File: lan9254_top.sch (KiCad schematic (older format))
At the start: 2 parts

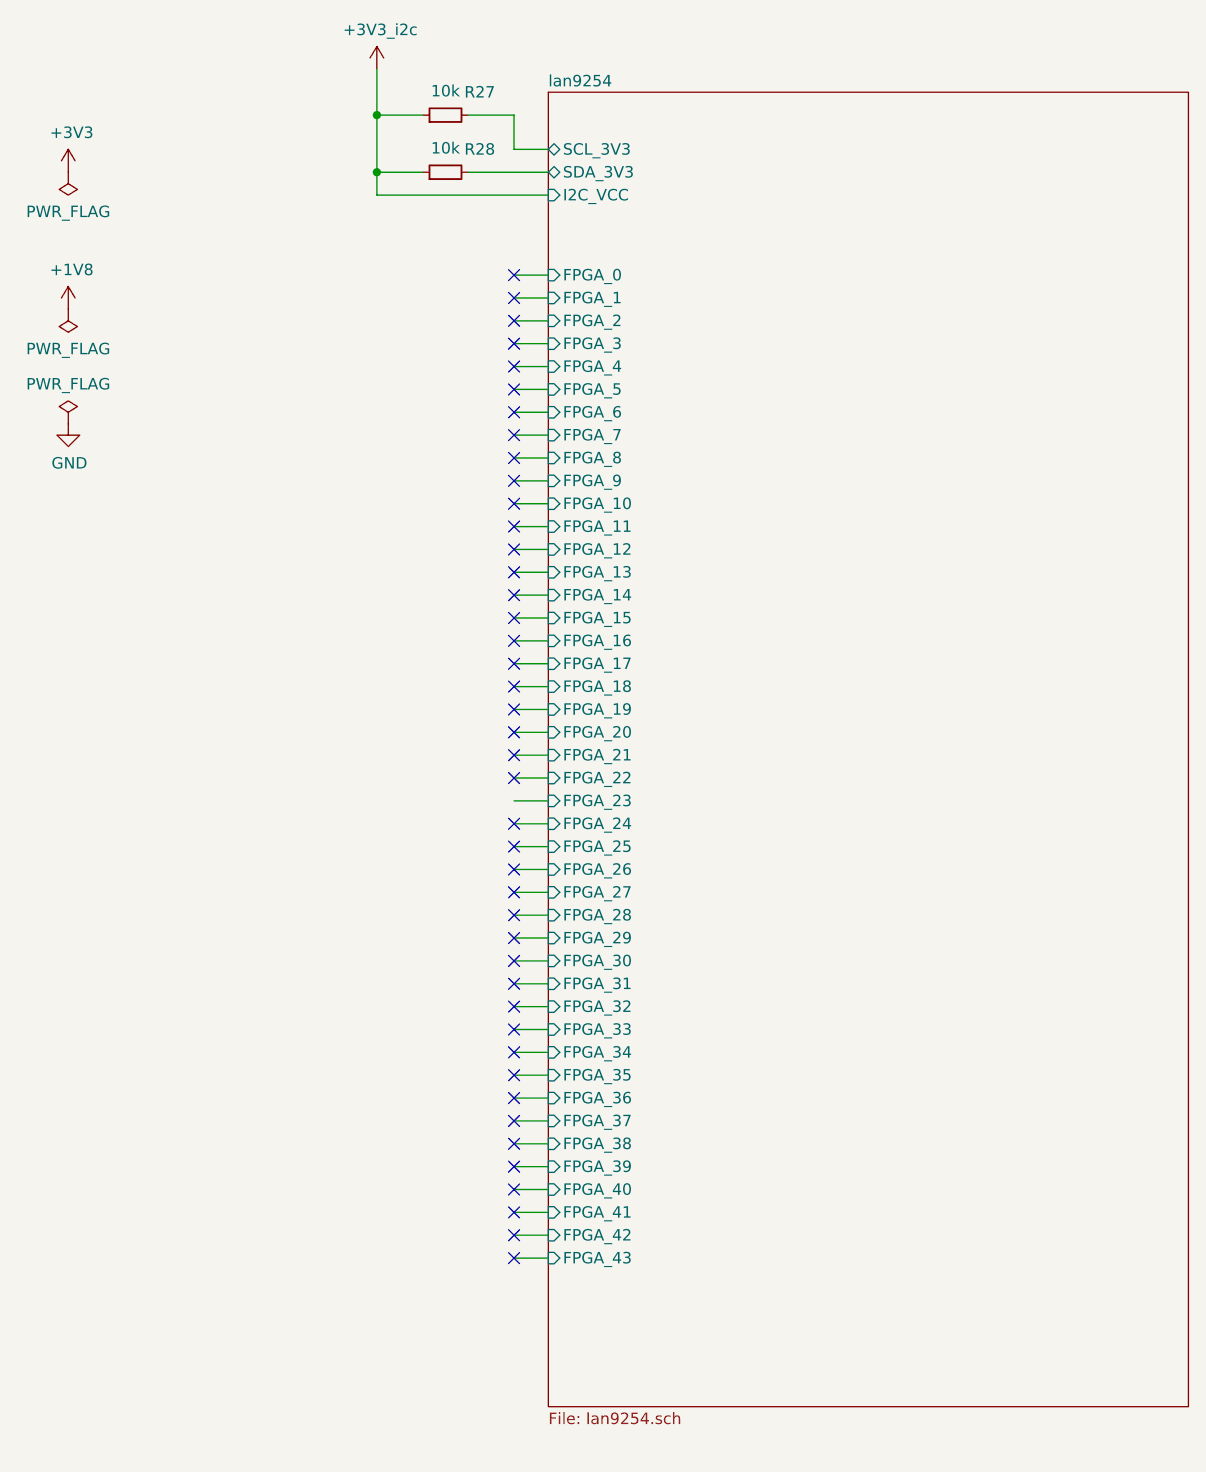
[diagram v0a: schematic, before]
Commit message: added I/O connectors, JTAG (just in case) and more
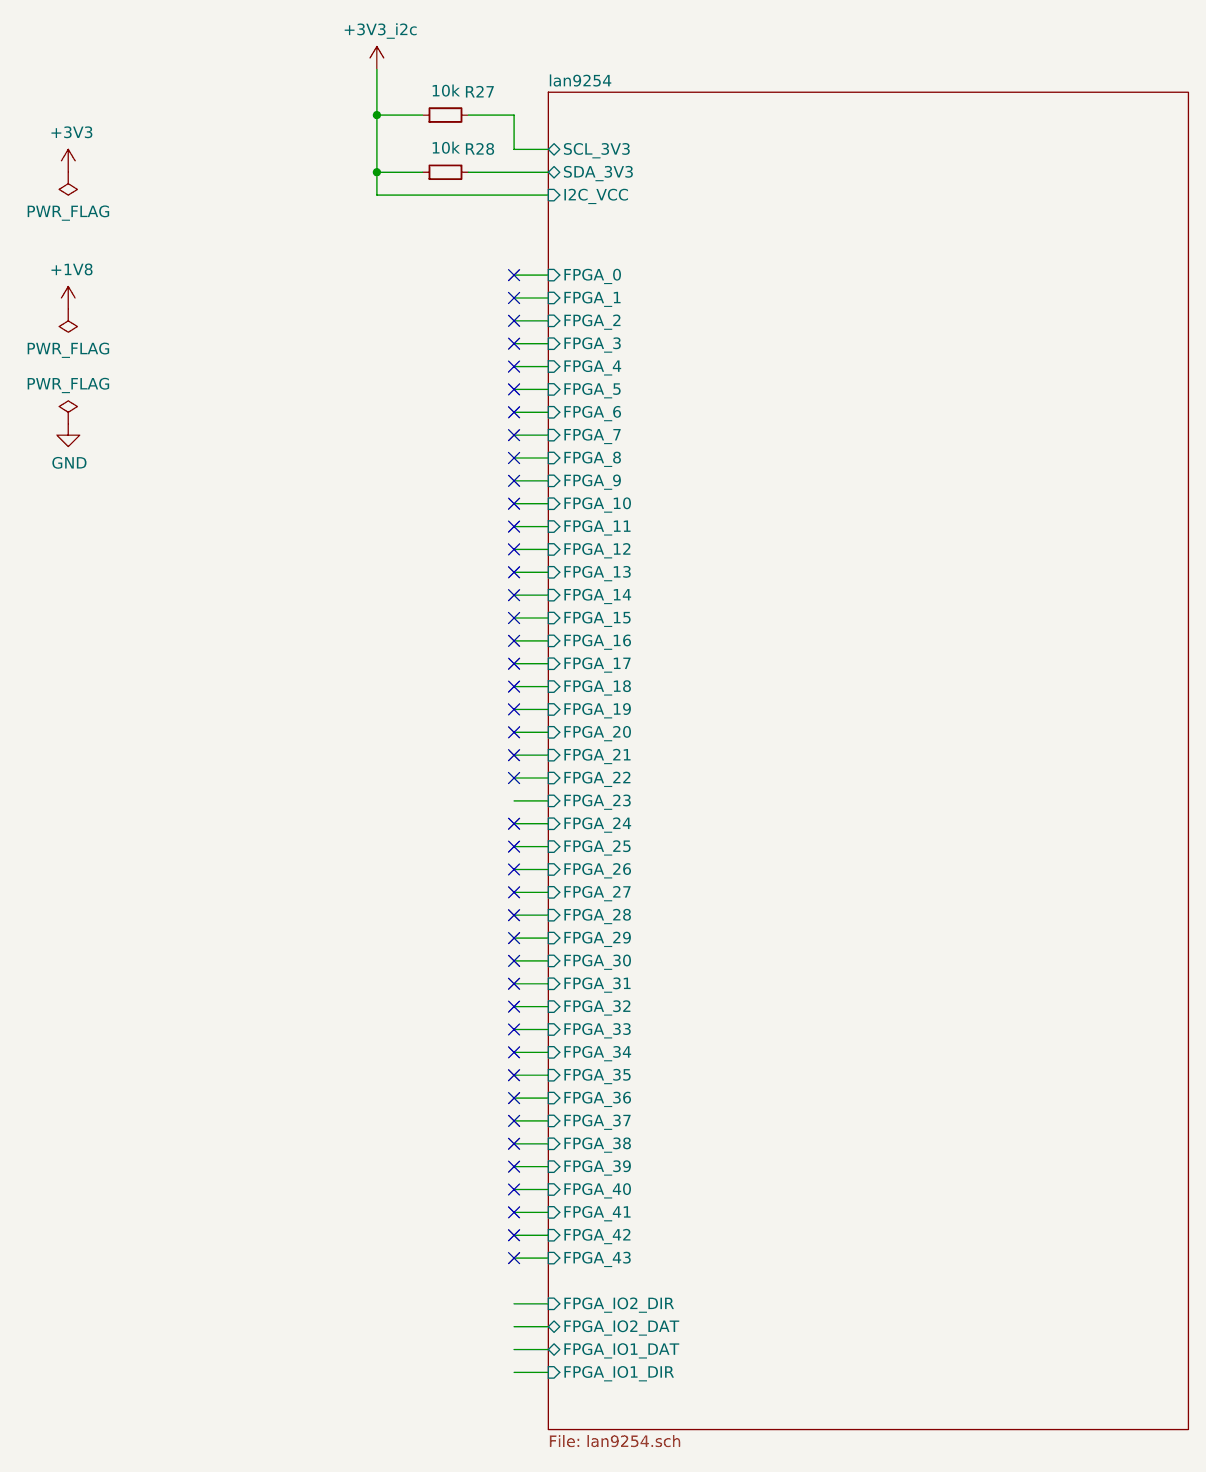
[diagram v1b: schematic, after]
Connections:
- wire segments 54 -> 58
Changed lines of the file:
@@
 $Descr A4 11693 8268
 encoding utf-8
-Sheet 1 4
+Sheet 1 6
 Title ""
 Date ""
@@
 	3150 1200 2950 1200
 $Sheet
-S 3300 1100 2800 5750
+S 3300 1100 2800 5850
 U 60DB2574
 F0 "lan9254" 50
@@
 F47 "FPGA_43" I L 3300 6200 50
 F48 "I2C_VCC" I L 3300 1550 50
+F49 "FPGA_IO2_DIR" I L 3300 6400 50
+F50 "FPGA_IO2_DAT" B L 3300 6500 50
+F51 "FPGA_IO1_DAT" B L 3300 6600 50
+F52 "FPGA_IO1_DIR" I L 3300 6700 50
 $EndSheet
 $Comp
@@
 	1    0    0    -1
 $EndComp
+Wire Wire Line
+	3150 6400 3300 6400
+Wire Wire Line
+	3150 6600 3300 6600
+Wire Wire Line
+	3150 6700 3300 6700
+Wire Wire Line
+	3300 6500 3150 6500
 $EndSCHEMATC

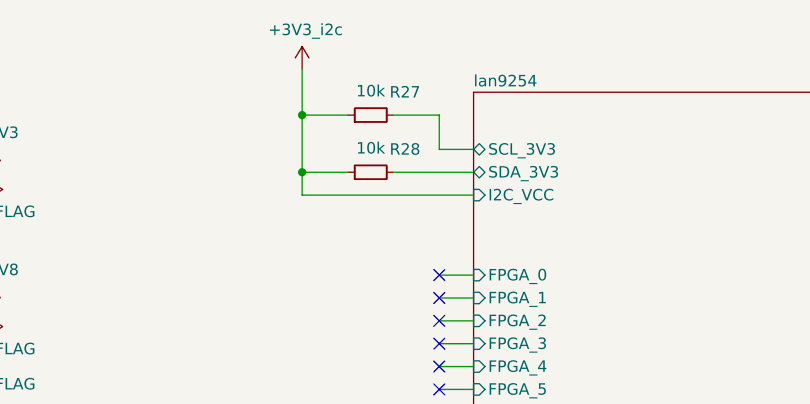
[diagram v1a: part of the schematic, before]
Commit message: reannotated top-module and updated PCB (prior to merging with base-board)
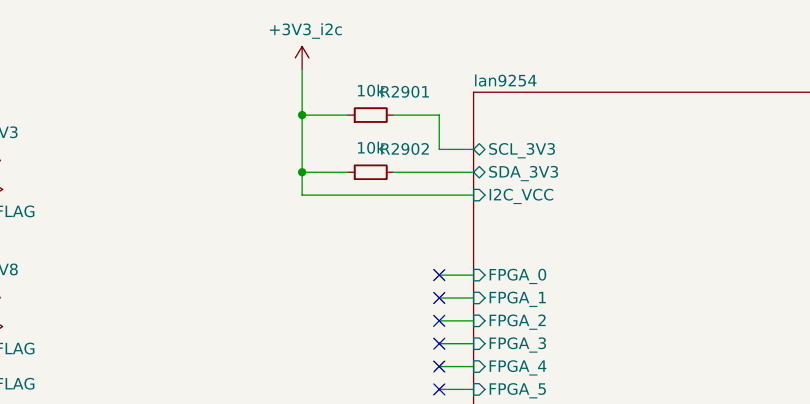
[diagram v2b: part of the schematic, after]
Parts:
- renumbered R27 to R2901, R28 to R2902
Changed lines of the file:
@@
 AR Path="/60E5E32B/6108B7FA" Ref="R?"  Part="1"
 AR Path="/60DB2574/60E5E32B/6108B7FA" Ref="R?"  Part="1"
-AR Path="/6108B7FA" Ref="R27"  Part="1"
-F 0 "R27" V 2950 1050 50  0000 C CNN
+AR Path="/6108B7FA" Ref="R2901"  Part="1"
+F 0 "R2901" V 2950 1050 50  0000 C CNN
 F 1 "10k" V 2955 1200 50  0000 C CNN
 F 2 "Resistor_SMD:R_0603_1608Metric" H 2850 1200 50  0001 C CNN
@@
 AR Path="/60E5E32B/6108C6EA" Ref="R?"  Part="1"
 AR Path="/60DB2574/60E5E32B/6108C6EA" Ref="R?"  Part="1"
-AR Path="/6108C6EA" Ref="R28"  Part="1"
-F 0 "R28" V 2950 1300 50  0000 C CNN
+AR Path="/6108C6EA" Ref="R2902"  Part="1"
+F 0 "R2902" V 2950 1300 50  0000 C CNN
 F 1 "10k" V 2955 1450 50  0000 C CNN
 F 2 "Resistor_SMD:R_0603_1608Metric" H 2850 1450 50  0001 C CNN
